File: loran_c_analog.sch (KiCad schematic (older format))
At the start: 54 parts, among them P601 DAC VCO, P602 DAC AGC, P603 LORAN In, P604 RSVD In, Q601 BD135, Q602 BD136, U601 TL072, U602 LD1117S33

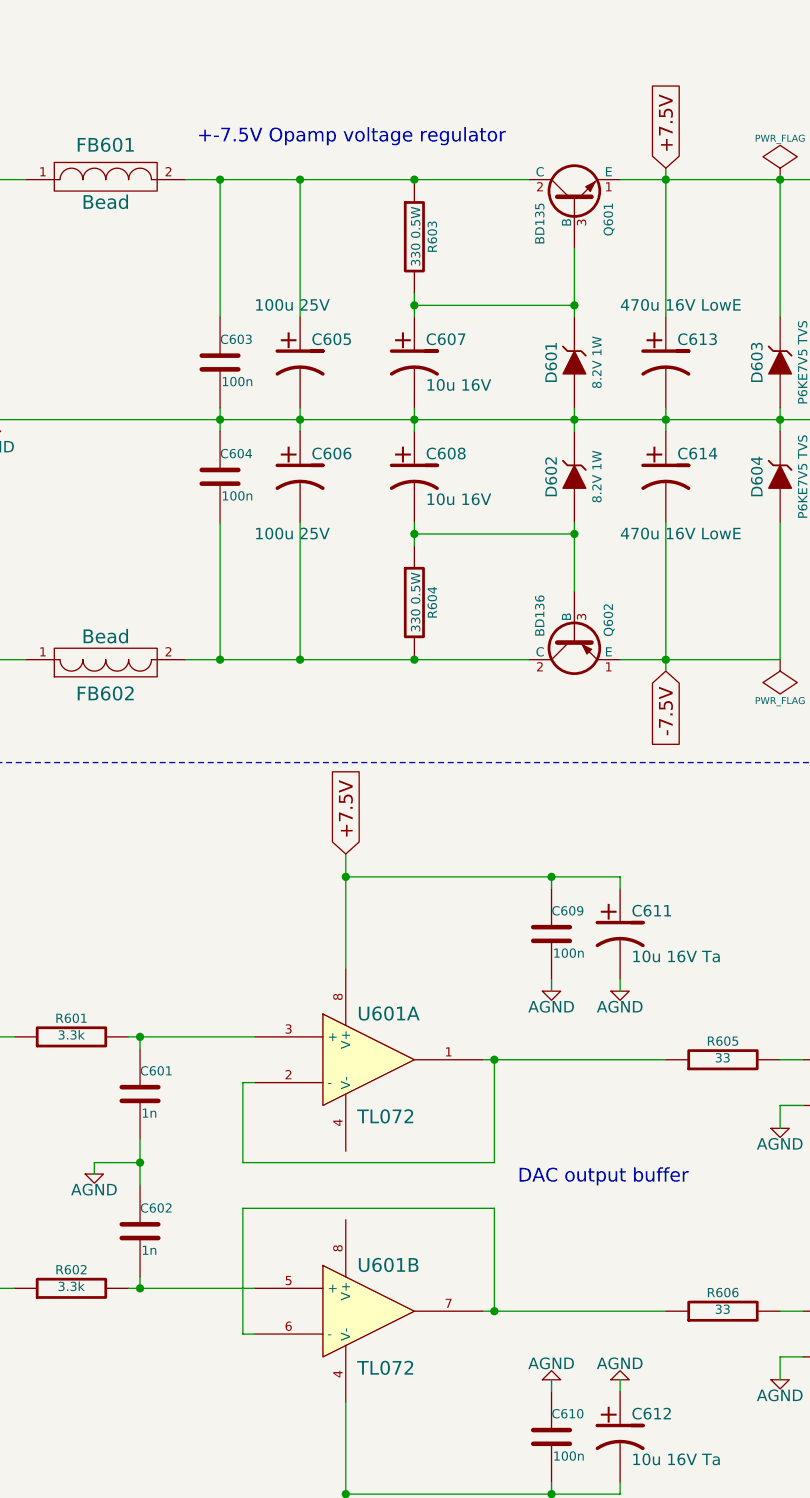
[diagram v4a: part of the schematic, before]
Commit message: Intermediate update: PCB routing/schematic tweaking in process..
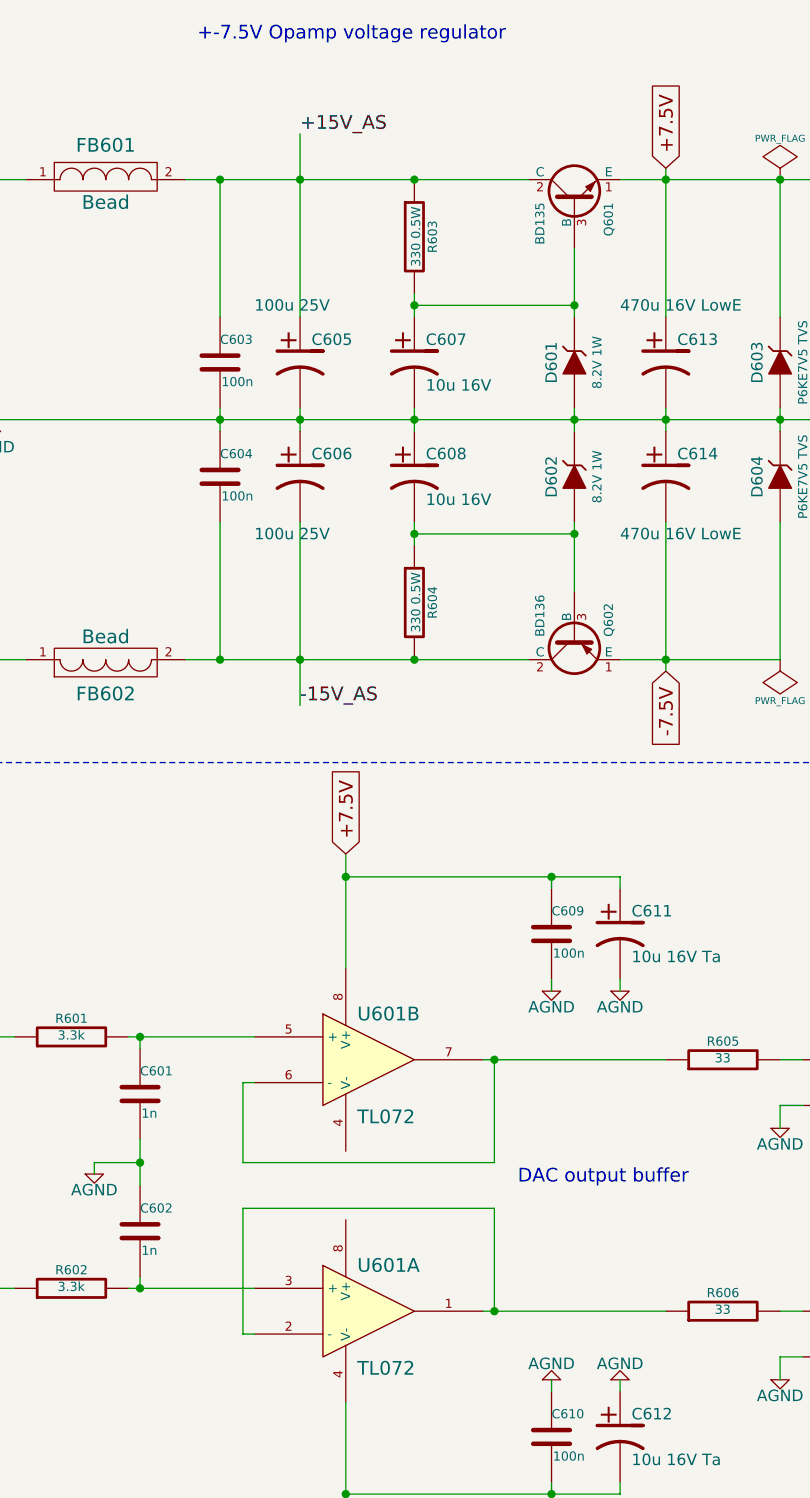
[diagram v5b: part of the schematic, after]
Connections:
- net +15V_AS: now reaches C603.1, C605.1, FB601.2, Q601.2 (C), R603.1
- net -15V_AS: now reaches C604.2, C606.2, FB602.2, Q602.2 (C), R604.2
- net at C601.1, R601.2: now also U601.5 (+); no longer U601.3 (+)
- net at C602.2, R602.2: now also U601.3 (+); no longer U601.5 (+)
- new net: R605.1, U601.6 (-), U601.7
- new net: R606.1, U601.1, U601.2 (-)
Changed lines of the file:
@@
 $EndComp
 $Comp
-L +3.3VADC #PWR0102
+L +3.3VADC #PWR0100
 U 1 1 52E38762
 P 7700 1650
-F 0 "#PWR0102" H 7700 1770 20  0001 C CNN
+F 0 "#PWR0100" H 7700 1770 20  0001 C CNN
 F 1 "+3.3VADC" H 7700 1740 30  0000 C CNN
 F 2 "" H 7700 1650 60  0000 C CNN
@@
 -7.5V
 $Comp
-L AGND #PWR0103
+L AGND #PWR0101
 U 1 1 52E3C710
 P 1150 2400
-F 0 "#PWR0103" H 1150 2400 40  0001 C CNN
+F 0 "#PWR0101" H 1150 2400 40  0001 C CNN
 F 1 "AGND" H 1150 2330 50  0000 C CNN
 F 2 "" H 1150 2400 60  0000 C CNN
@@
 $Comp
 L TL072 U601
-U 1 1 52E3D0CB
+U 2 1 52E3D0CB
 P 2800 5150
 F 0 "U601" H 2750 5350 60  0000 L CNN
@@
 F 2 "w_pth_ic:dil_8-300" H 2800 5150 60  0001 C CNN
 F 3 "" H 2800 5150 60  0000 C CNN
-	1    2800 5150
+	2    2800 5150
 	1    0    0    -1
 $EndComp
 $Comp
 L TL072 U601
-U 2 1 52E3D0DD
+U 1 1 52E3D0DD
 P 2800 6250
 F 0 "U601" H 2750 6450 60  0000 L CNN
@@
 F 2 "w_pth_ic:dil_8-300" H 2800 6250 60  0001 C CNN
 F 3 "" H 2800 6250 60  0000 C CNN
-	2    2800 6250
+	1    2800 6250
 	1    0    0    -1
 $EndComp
@@
 $EndComp
 $Comp
-L AGND #PWR0104
+L AGND #PWR0102
 U 1 1 52E42BA3
 P 3600 4850
-F 0 "#PWR0104" H 3600 4850 40  0001 C CNN
+F 0 "#PWR0102" H 3600 4850 40  0001 C CNN
 F 1 "AGND" H 3600 4780 50  0000 C CNN
 F 2 "" H 3600 4850 60  0000 C CNN
@@
 $EndComp
 $Comp
-L AGND #PWR0105
+L AGND #PWR0103
 U 1 1 52E42BAE
 P 3900 4850
-F 0 "#PWR0105" H 3900 4850 40  0001 C CNN
+F 0 "#PWR0103" H 3900 4850 40  0001 C CNN
 F 1 "AGND" H 3900 4780 50  0000 C CNN
 F 2 "" H 3900 4850 60  0000 C CNN
@@
 $EndComp
 $Comp
-L AGND #PWR0106
+L AGND #PWR0104
 U 1 1 52E434DA
 P 3600 6550
-F 0 "#PWR0106" H 3600 6550 40  0001 C CNN
+F 0 "#PWR0104" H 3600 6550 40  0001 C CNN
 F 1 "AGND" H 3600 6480 50  0000 C CNN
 F 2 "" H 3600 6550 60  0000 C CNN
@@
 $EndComp
 $Comp
-L AGND #PWR0107
+L AGND #PWR0105
 U 1 1 52E434E0
 P 3900 6550
-F 0 "#PWR0107" H 3900 6550 40  0001 C CNN
+F 0 "#PWR0105" H 3900 6550 40  0001 C CNN
 F 1 "AGND" H 3900 6480 50  0000 C CNN
 F 2 "" H 3900 6550 60  0000 C CNN
@@
 $EndComp
 $Comp
-L PWR_FLAG #FLG0108
+L PWR_FLAG #FLG0106
 U 1 1 52E43900
 P 4600 1300
-F 0 "#FLG0108" H 4600 1395 30  0001 C CNN
+F 0 "#FLG0106" H 4600 1395 30  0001 C CNN
 F 1 "PWR_FLAG" H 4600 1480 30  0000 C CNN
 F 2 "" H 4600 1300 60  0000 C CNN
@@
 $EndComp
 $Comp
-L PWR_FLAG #FLG0109
+L PWR_FLAG #FLG0107
 U 1 1 52E4390B
 P 4600 3400
-F 0 "#FLG0109" H 4600 3495 30  0001 C CNN
+F 0 "#FLG0107" H 4600 3495 30  0001 C CNN
 F 1 "PWR_FLAG" H 4600 3580 30  0000 C CNN
 F 2 "" H 4600 3400 60  0000 C CNN
@@
 $EndComp
 $Comp
-L AGND #PWR0110
+L AGND #PWR0108
 U 1 1 52E4434F
 P 4600 5450
-F 0 "#PWR0110" H 4600 5450 40  0001 C CNN
+F 0 "#PWR0108" H 4600 5450 40  0001 C CNN
 F 1 "AGND" H 4600 5380 50  0000 C CNN
 F 2 "" H 4600 5450 60  0000 C CNN
@@
 $EndComp
 $Comp
-L AGND #PWR0111
+L AGND #PWR0109
 U 1 1 52E4435A
 P 4600 6550
-F 0 "#PWR0111" H 4600 6550 40  0001 C CNN
+F 0 "#PWR0109" H 4600 6550 40  0001 C CNN
 F 1 "AGND" H 4600 6480 50  0000 C CNN
 F 2 "" H 4600 6550 60  0000 C CNN
@@
 $EndComp
 $Comp
-L AGND #PWR0112
+L AGND #PWR0110
 U 1 1 52E476C2
 P 1600 5650
-F 0 "#PWR0112" H 1600 5650 40  0001 C CNN
+F 0 "#PWR0110" H 1600 5650 40  0001 C CNN
 F 1 "AGND" H 1600 5580 50  0000 C CNN
 F 2 "" H 1600 5650 60  0000 C CNN
@@
 	1    0    0    -1
 $EndComp
-Text Notes 2050 1150 0    60   ~ 0
+Text Notes 2050 700  0    60   ~ 0
 +-7.5V Opamp voltage regulator
 $Comp
@@
 $EndComp
 $Comp
-L AGND #PWR0113
+L AGND #PWR0111
 U 1 1 52E4B7B5
 P 7950 4100
-F 0 "#PWR0113" H 7950 4100 40  0001 C CNN
+F 0 "#PWR0111" H 7950 4100 40  0001 C CNN
 F 1 "AGND" H 7950 4030 50  0000 C CNN
 F 2 "" H 7950 4100 60  0000 C CNN
@@
 $EndComp
 $Comp
-L AGND #PWR0114
+L AGND #PWR0112
 U 1 1 52E4C26B
 P 8450 4100
-F 0 "#PWR0114" H 8450 4100 40  0001 C CNN
+F 0 "#PWR0112" H 8450 4100 40  0001 C CNN
 F 1 "AGND" H 8450 4030 50  0000 C CNN
 F 2 "" H 8450 4100 60  0000 C CNN
@@
 $EndComp
 $Comp
-L AGND #PWR0115
+L AGND #PWR0113
 U 1 1 52E4D87E
 P 8200 4100
-F 0 "#PWR0115" H 8200 4100 40  0001 C CNN
+F 0 "#PWR0113" H 8200 4100 40  0001 C CNN
 F 1 "AGND" H 8200 4030 50  0000 C CNN
 F 2 "" H 8200 4100 60  0000 C CNN
@@
 $EndComp
 $Comp
-L AGND #PWR0116
+L AGND #PWR0114
 U 1 1 52E4EBFE
 P 9100 4100
-F 0 "#PWR0116" H 9100 4100 40  0001 C CNN
+F 0 "#PWR0114" H 9100 4100 40  0001 C CNN
 F 1 "AGND" H 9100 4030 50  0000 C CNN
 F 2 "" H 9100 4100 60  0000 C CNN
@@
 $EndComp
 $Comp
-L AGND #PWR0117
+L AGND #PWR0115
 U 1 1 52E4EC09
 P 9400 4100
-F 0 "#PWR0117" H 9400 4100 40  0001 C CNN
+F 0 "#PWR0115" H 9400 4100 40  0001 C CNN
 F 1 "AGND" H 9400 4030 50  0000 C CNN
 F 2 "" H 9400 4100 60  0000 C CNN
@@
 $EndComp
 $Comp
-L +3.3VADC #PWR0118
+L +3.3VADC #PWR0116
 U 1 1 52E4EC14
 P 9100 2750
-F 0 "#PWR0118" H 9100 2870 20  0001 C CNN
+F 0 "#PWR0116" H 9100 2870 20  0001 C CNN
 F 1 "+3.3VADC" H 9100 2840 30  0000 C CNN
 F 2 "" H 9100 2750 60  0000 C CNN
@@
 $EndComp
 $Comp
-L AGND #PWR0119
+L AGND #PWR0117
 U 1 1 52E53548
 P 10250 4100
-F 0 "#PWR0119" H 10250 4100 40  0001 C CNN
+F 0 "#PWR0117" H 10250 4100 40  0001 C CNN
 F 1 "AGND" H 10250 4030 50  0000 C CNN
 F 2 "" H 10250 4100 60  0000 C CNN
@@
 $EndComp
 $Comp
-L AGND #PWR0120
+L AGND #PWR0118
 U 1 1 52E545C4
 P 7950 5900
-F 0 "#PWR0120" H 7950 5900 40  0001 C CNN
+F 0 "#PWR0118" H 7950 5900 40  0001 C CNN
 F 1 "AGND" H 7950 5830 50  0000 C CNN
 F 2 "" H 7950 5900 60  0000 C CNN
@@
 $EndComp
 $Comp
-L AGND #PWR0121
+L AGND #PWR0119
 U 1 1 52E545D0
 P 8450 5900
-F 0 "#PWR0121" H 8450 5900 40  0001 C CNN
+F 0 "#PWR0119" H 8450 5900 40  0001 C CNN
 F 1 "AGND" H 8450 5830 50  0000 C CNN
 F 2 "" H 8450 5900 60  0000 C CNN
@@
 $EndComp
 $Comp
-L AGND #PWR0122
+L AGND #PWR0120
 U 1 1 52E545EF
 P 8200 5900
-F 0 "#PWR0122" H 8200 5900 40  0001 C CNN
+F 0 "#PWR0120" H 8200 5900 40  0001 C CNN
 F 1 "AGND" H 8200 5830 50  0000 C CNN
 F 2 "" H 8200 5900 60  0000 C CNN
@@
 $EndComp
 $Comp
-L AGND #PWR0123
+L AGND #PWR0121
 U 1 1 52E54601
 P 9100 5900
-F 0 "#PWR0123" H 9100 5900 40  0001 C CNN
+F 0 "#PWR0121" H 9100 5900 40  0001 C CNN
 F 1 "AGND" H 9100 5830 50  0000 C CNN
 F 2 "" H 9100 5900 60  0000 C CNN
@@
 $EndComp
 $Comp
-L AGND #PWR0124
+L AGND #PWR0122
 U 1 1 52E54607
 P 9400 5900
-F 0 "#PWR0124" H 9400 5900 40  0001 C CNN
+F 0 "#PWR0122" H 9400 5900 40  0001 C CNN
 F 1 "AGND" H 9400 5830 50  0000 C CNN
 F 2 "" H 9400 5900 60  0000 C CNN
@@
 $EndComp
 $Comp
-L +3.3VADC #PWR0125
+L +3.3VADC #PWR0123
 U 1 1 52E5460D
 P 9100 4550
-F 0 "#PWR0125" H 9100 4670 20  0001 C CNN
+F 0 "#PWR0123" H 9100 4670 20  0001 C CNN
 F 1 "+3.3VADC" H 9100 4640 30  0000 C CNN
 F 2 "" H 9100 4550 60  0000 C CNN
@@
 $EndComp
 $Comp
-L AGND #PWR0126
+L AGND #PWR0124
 U 1 1 52E54639
 P 10250 5900
-F 0 "#PWR0126" H 10250 5900 40  0001 C CNN
+F 0 "#PWR0124" H 10250 5900 40  0001 C CNN
 F 1 "AGND" H 10250 5830 50  0000 C CNN
 F 2 "" H 10250 5900 60  0000 C CNN
@@
 Connection ~ 3000 2350
 Wire Wire Line
-	2500 1900 2500 1300
+	2500 1100 2500 1900
 Wire Wire Line
 	2150 1900 2150 1300
@@
 	2000 3400 3500 3400
 Wire Wire Line
-	2500 2800 2500 3400
+	2500 2800 2500 3600
 Wire Wire Line
 	2150 2800 2150 3400
@@
 Text Notes 7900 6300 0    60   ~ 0
 Rt: line termination load
+Text Label 2500 1100 0    60   ~ 0
++15V_AS
+Text Label 2500 3600 0    60   ~ 0
+-15V_AS
 $EndSCHEMATC

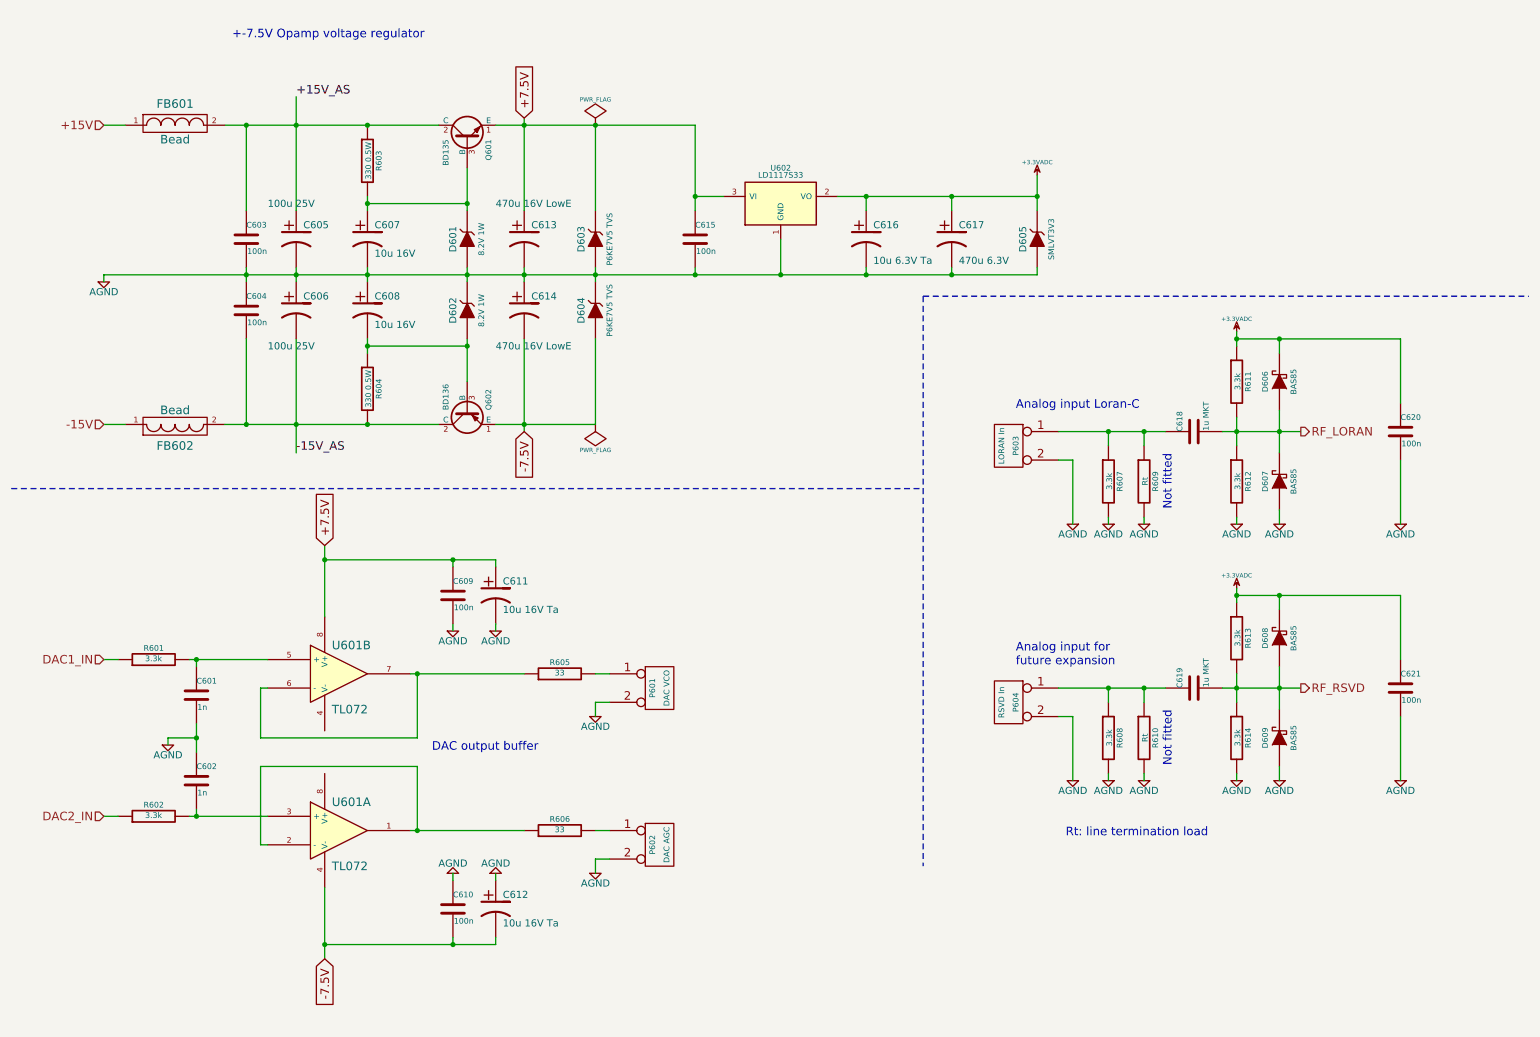
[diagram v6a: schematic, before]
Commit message: Update: lots of refactoring and pin remap ..In chase for easier PCB routing PCB still not completed
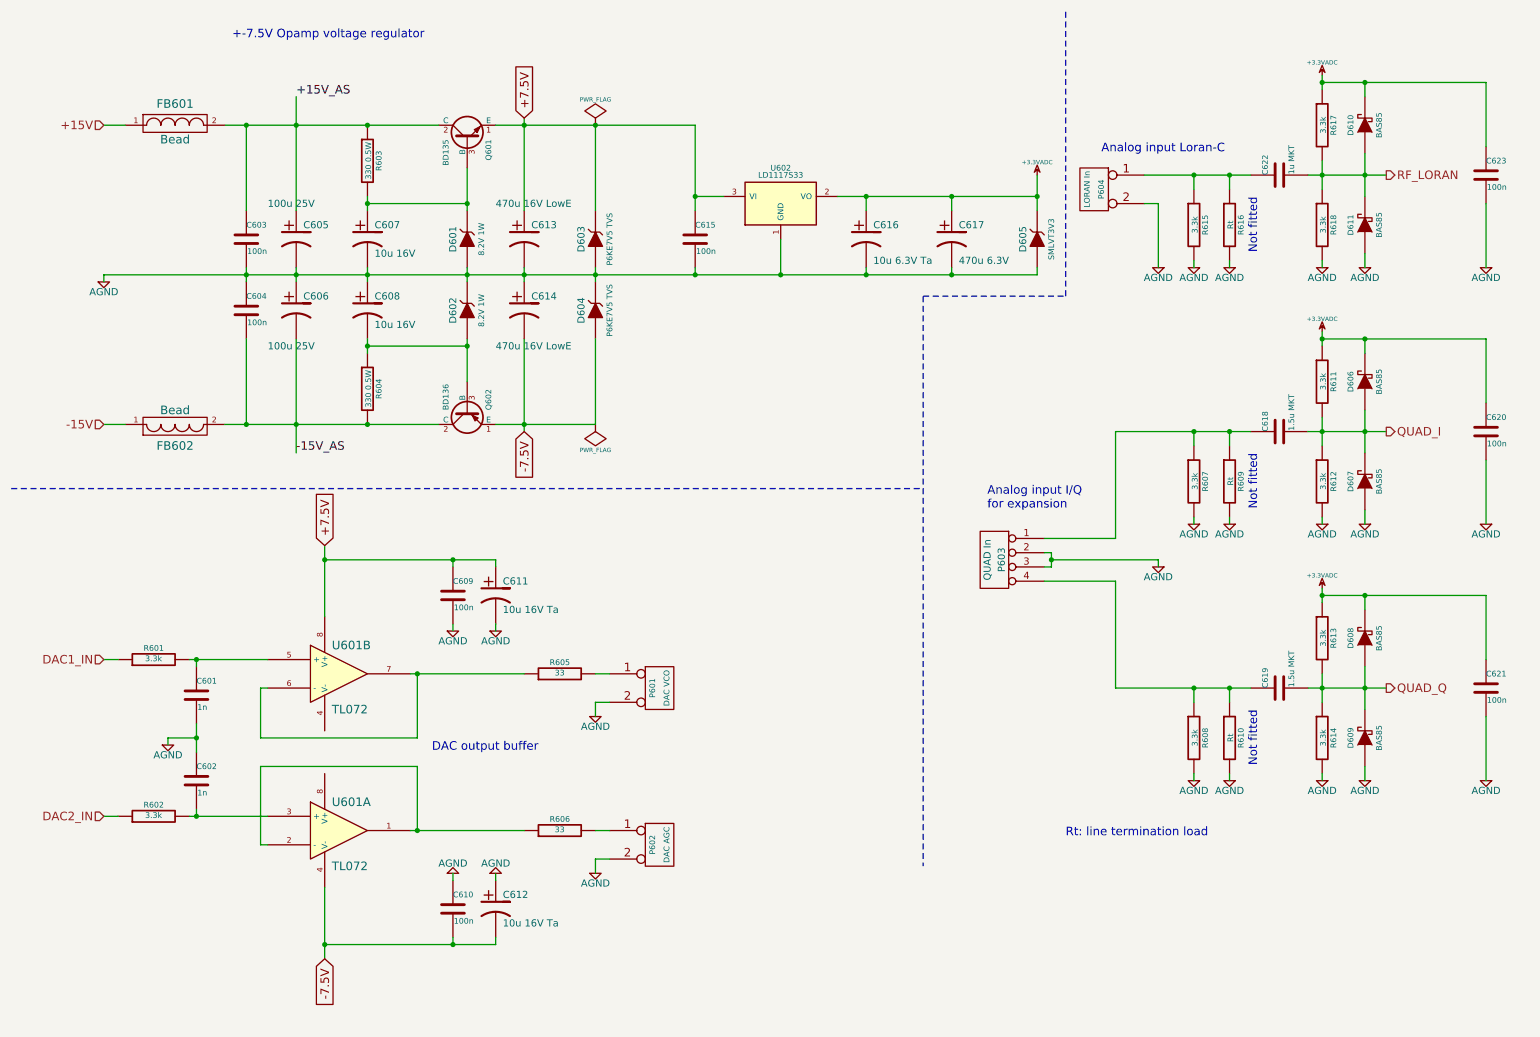
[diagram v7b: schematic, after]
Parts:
- removed P603: LORAN In, w_conn_kk100:kk100_22-23-2021, symbol CONN_2
- added C622: 1u MKT, w_pth_capacitors:cnp_7x6mm, symbol C
- added C623: 100n, w_smd_capacitors:c_1206, symbol C
- added D610, D611: BAS85, w_smd_diode:sod80c, symbol DIODESCH
- added P603: QUAD In, symbol CONN_4
- added R615, R617, R618: 3.3k, w_smd_resistors:r_1206, symbol R
- added R616: Rt, w_pth_resistors:RC07, symbol R
- C618, C619: value 1u MKT -> 1.5u MKT
- P604: value RSVD In -> LORAN In
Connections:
- net +3.3VADC: now also C623.1, D610.2 (K), R617.1
- net AGND: now also C623.2, D611.1 (A), P603.2 (P2), P603.3 (P3), R615.2, R616.2, R618.2
- net RF_LORAN: now also C622.2, D610.1 (A), D611.2 (K), R617.2, R618.1; no longer C618.2, D606.1 (A), D607.2 (K), R611.2, R612.1
- net at C618.1, R607.1, R609.1: now also P603.1 (P1)
- net at C619.1, R608.1, R610.1: now also P603.4 (P4); no longer P604.1 (P1)
- net RF_RSVD renamed QUAD_Q
- new net: C622.1, P604.1 (P1), R615.1, R616.1
- new net QUAD_I: C618.2, D606.1 (A), D607.2 (K), R611.2, R612.1
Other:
- note added: "Analog input I/Q\nfor expansion"
- note removed: "Analog input for\nfuture expansion"
- moved on the sheet: C618, C619, C620, C621, D606, D607, D608, D609, R607, R608, R609, R610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
